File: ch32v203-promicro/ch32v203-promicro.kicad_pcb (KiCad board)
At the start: 2 copper layers, 17.8 x 33 mm, 27 parts, among them J1 USB2.0_C_v3, J2 ProMicro-LeftPin, J3 ProMicro-RightPin, SW1 SW_Push, SW2 SW_Push, U1 CH32V203CxT6, U2 AMS1117-3.3, Y1 32.768k, Y2 8M

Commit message: stm32
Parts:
- added JP1: Jumper_3_Open, Jumper:SolderJumper-3_P1.3mm_Open_RoundedPad1.0x1.5mm, B.Cu at (113.9, 128.3)
- added R8: 10k, $74th:Register_0805_2012, B.Cu at (106.2, 127.6)
- J2: value ProMicro-LeftPin -> ProMicro-LeftPin-NoGND; footprint $74th:ProMicro_LIKE_LEFT -> $74th:ProMicro_LIKE_LEFT_NO_GND
- moved C6 4.83 mm to (109.0, 125.7)
- moved R1 1.81 mm to (106.2, 109.9)
- moved C10 1.27 mm to (113.4, 131.9), turned to 0 degrees
- moved R2 0.86 mm to (112.7, 124.9), turned to 180 degrees
- moved R6 0.46 mm to (103.1, 124.4)
- moved C5 0.35 mm to (108.1, 112.8)
- moved R7 0.35 mm to (106.0, 124.4)
- moved Y2 0.32 mm to (109.0, 130.8)
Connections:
- J2 pad 3: GND -> SWDIO
- J2 pad 4: GND -> SWCLK
- SW1 pad 1: GND -> Net-(JP1-C)
- U1 pad 14: unconnected-(U1-Pad14) -> 10/A10
- U1 pad 34: unconnected-(U1-Pad34) -> SWDIO
- U1 pad 37: unconnected-(U1-Pad37) -> SWCLK
- U1 pad 38: 10/A10 -> unconnected-(U1-PA15-Pad38)
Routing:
- net 10/A10: track 25.2 -> 12.3 mm, vias 1 -> 2
- net GND: track 98.7 -> 86.5 mm, vias 25 -> 23
- net SWDIO: track 0.00 -> 9.83 mm
- net Net-(JP1-C): track 0.00 -> 7.83 mm, vias 0 -> 1
- net SWCLK: track 0.00 -> 7.28 mm
- net RST: track 36.6 -> 40.3 mm, vias 1 -> 3
- net +3V3: track 64.4 -> 67.1 mm
- net Net-(U1-VDDA): track 4.69 -> 2.70 mm
- net 1/UART_TX: track 15.2 -> 16.5 mm
- net DP: track 25.5 -> 24.4 mm
- net 0/UART_RX: track 12.8 -> 13.8 mm
- net Net-(D1-A): track 2.19 -> 2.91 mm
- net 19/A1: track 9.64 -> 10.2 mm
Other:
- board text added: "B"
- board text added: "SELECT BOOT0 R2:3V3 R8:GND"
- board text added: "STM32Micro"
- board text added: "V"
- board text removed: "C32V203Micro"

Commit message: stm32
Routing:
- net GND: track 86.5 -> 89.1 mm
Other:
- board text added: "A4"
- board text added: "A5"
- board text added: "TX1 RX1"
- board text removed: "A15"
- board text removed: "AD0"
- board text removed: "AD1"
- board text removed: "AD2"
- board text removed: "AD3"
- board text removed: "MISO"
- board text removed: "MOSI"
- board text removed: "RX"
- board text removed: "SCK"
- board text removed: "SPI1"
- board text removed: "TX"
- board text removed: "UART1"

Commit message: stm32
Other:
- board text added: "v1.1.0"
- board text removed: "v1.0.0"
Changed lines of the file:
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@@
   (gr_arc (start 101.279026 133.010974) (mid 100.381 132.639) (end 100.009026 131.740974)
     (stroke (width 0.1) (type solid)) (layer "Edge.Cuts"))
-  (gr_text "v1.0.0" (at 111.8 108.7) (layer "B.SilkS")
+  (gr_text "v1.1.0" (at 111.8 108.7) (layer "B.SilkS")
     (effects (font (size 1 1) (thickness 0.15)) (justify mirror))
   )

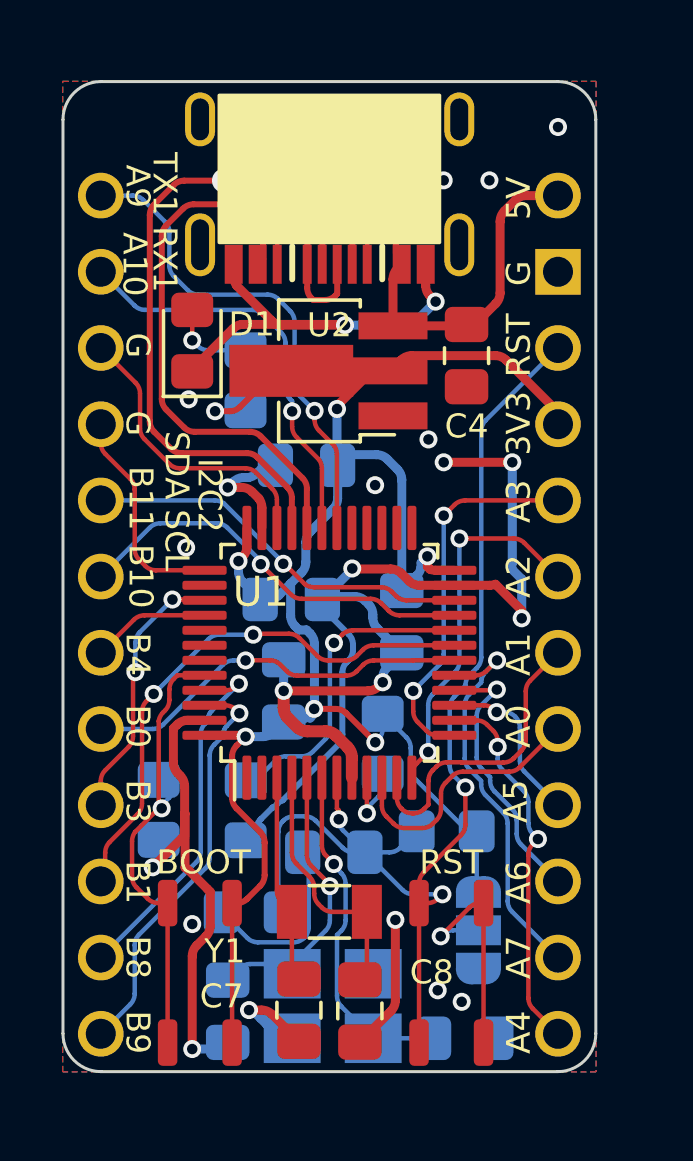
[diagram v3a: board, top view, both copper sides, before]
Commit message: x32micro v1.1.0
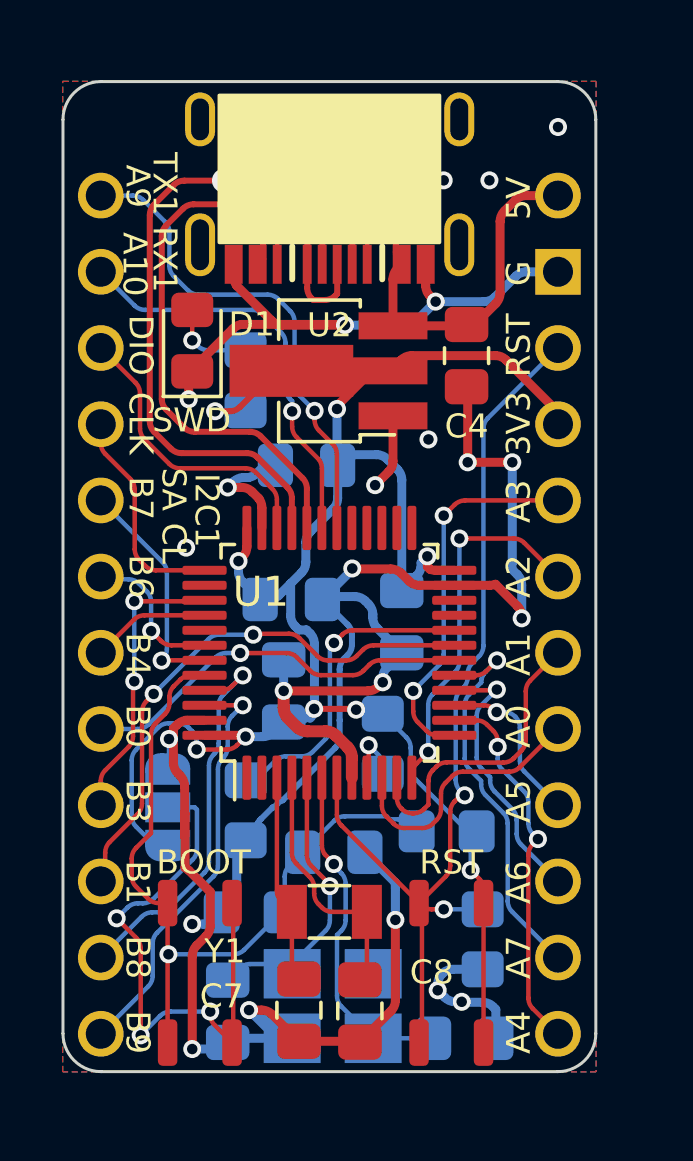
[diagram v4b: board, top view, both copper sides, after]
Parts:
- added REF**: JLCJLCJLCJLC, $74th:JLCJLCJLCJLC, B.Cu at (103.1, 104.4)
- U1: value CH32V203CxT6 -> STM32V103C8T6
- moved R6 11.6 mm to (113.9, 128.7)
- moved JP1 11.1 mm to (103.5, 124.2), turned to -90 degrees
- turned C6 to 0 degrees
- turned SW2 to -90 degrees
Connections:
- net Net-(U1-BOOT1/PB2/UART4_CK) renamed BOOT1
- C6 pad 1: RST -> BOOT0
- R2 pad 2: RST -> BOOT0
- R6 pad 1: Net-(U1-BOOT0) -> RST
- R8 pad 1: RST -> BOOT0
- SW1 pad 1: Net-(JP1-C) -> +3V3
- SW2 pad 1: Net-(U1-BOOT0) -> Net-(JP1-C)
- SW2 pad 2: +3V3 -> BOOT0
- U1 pad 21: 3/I2C_SCL -> unconnected-(U1-PB10/I2C2_SCL/UART3_TX-Pad21)
- U1 pad 22: 2/I2C_SDA -> unconnected-(U1-PB11/I2C2_SDA/UART3_RX-Pad22)
- U1 pad 42: unconnected-(U1-PB6/USB2DM/I2C1_SCL-Pad42) -> 3/I2C_SCL
- U1 pad 43: unconnected-(U1-PB7/USB2DP/I2C1_SDA-Pad43) -> 2/I2C_SDA
- U1 pad 44: Net-(U1-BOOT0) -> BOOT0
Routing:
- net BOOT0: track 0.00 -> 25.0 mm, vias 0 -> 1
- net GND: track 89.1 -> 110.5 mm
- net Net-(U1-BOOT0): track 15.6 -> 0.00 mm, vias 1 -> 0
- net Net-(JP1-C): track 7.83 -> 18.8 mm, vias 1 -> 3
- net 3/I2C_SCL: track 13.7 -> 5.02 mm
- net RST: track 40.3 -> 32.8 mm, vias 3 -> 2
- net 2/I2C_SDA: track 13.1 -> 7.71 mm
- net +3V3: track 67.1 -> 68.5 mm, vias 7 -> 9
- net 8/A8: track 12.2 -> 13.0 mm
- net 6/A7: track 8.85 -> 9.59 mm
- net Net-(U1-PC15/OSC32OUT): track 9.22 -> 8.54 mm
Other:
- board text added: "+"
- board text added: "@74th"
- board text added: "B6"
- board text added: "B7"
- board text added: "BT0Pull R2:3V3 R8:GND"
- board text added: "BTBtn"
- board text added: "CL"
- board text added: "CLK"
- board text added: "DIO"
- board text added: "I2C1"
- board text added: "SA"
- board text added: "SWD"
- board text added: "X32Micro"
- board text added: ""
- board text removed: "B"
- board text removed: "B10"
- board text removed: "B11"
- board text removed: "I2C2"
- board text removed: "SCL"
- board text removed: "SDA"
- board text removed: "SELECT BOOT0 R2:3V3 R8:GND"
- board text removed: "STM32Micro"
- board text removed: "V"

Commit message: v1.2.0
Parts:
- removed C8: 12p, $74th:Capacitor_0805_2012
- removed J2: ProMicro-LeftPin-NoGND, $74th:ProMicro_LIKE_LEFT_NO_GND
- removed J3: ProMicro-RightPin, $74th:ProMicro_LIKE_RIGHT
- removed JP1: Jumper_3_Open, Jumper:SolderJumper-3_P1.3mm_Open_RoundedPad1.0x1.5mm
- removed R3: 0, $74th:Register_0805_2012
- removed R6: 10k, $74th:Register_0805_2012
- removed Y1: 32.768k, $74th:Crystal_SMD_3215-2Pin_3.2x1.5mm
- added C11: 1u, $74th:Capacitor_0805_2012, B.Cu at (110.4, 115.1)
- added J5: ProMicro-LeftPin-NoGND, $74th:ProMicro_LIKE_LEFT_NO_GND, F.Cu at (101.6, 118.1)
- added J6: ProMicro-RightPin, $74th:ProMicro_LIKE_RIGHT, F.Cu at (116.8, 119.4)
- added R9: 27.4, $74th:Register_0805_2012, B.Cu at (108.7, 109.8)
- added U4: CH213K, Package_TO_SOT_SMD:SOT-23, B.Cu at (107.1, 102.5)
- C5: value 2.2u -> 10u
- C7: value 12p -> 100n; moved to B.Cu
- D1: value LED -> BLUE
- R1: value 200 -> 10k
- R2: value 10k -> 27.4
- moved R2 15.2 mm to (110.6, 109.8), turned to -90 degrees
- moved C7 13.6 mm to (107.6, 117.4), turned to 0 degrees
- moved R7 9.70 mm to (113.4, 118.1), turned to 90 degrees
- moved C4 9.55 mm to (103.9, 109.8)
- moved D1 9.28 mm to (113.6, 109.0)
- moved R1 7.44 mm to (113.6, 109.0)
- moved C6 6.06 mm to (113.5, 129.8)
- moved C2 5.75 mm to (111.6, 121.4)
- moved C5 5.42 mm to (113.5, 112.2), turned to 0 degrees
- moved R8 4.32 mm to (103.5, 131.0), turned to -90 degrees
- moved R4 1.99 mm to (109.9, 103.0)
- moved R5 1.90 mm to (111.8, 103.0)
- moved C3 0.82 mm to (107.6, 121.1)
- moved U2 0.54 mm to (109.0, 110.2), turned to 0 degrees
- moved SW1 0.47 mm to (113.3, 130.0)
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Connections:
- net BOOT1 renamed Net-(U1-BOOT1/PB2)
- C4 pad 1: +5V -> Net-(U2-VI)
- C6 pad 1: BOOT0 -> /~{RESET}
- C7 pad 1: Net-(U1-PC14/OSC32IN) -> +3V3
- J1 pad 2: DM -> Net-(J1-D-)
- J1 pad 3: DP -> Net-(J1-D+)
- R2 pad 1: +3V3 -> Net-(J1-D-)
- R2 pad 2: BOOT0 -> /USB_DM
- R8 pad 1: BOOT0 -> Net-(U1-BOOT0)
- SW1 pad 2: RST -> /~{RESET}
- SW2 pad 1: Net-(JP1-C) -> +3V3
- SW2 pad 2: BOOT0 -> Net-(U1-BOOT0)
- U1 pad 1: unconnected-(U1-VBAT-Pad1) -> +3V3
- U1 pad 10: 18/A0 -> /18/A0
- U1 pad 11: 19/A1 -> /19/A1
- U1 pad 12: 20/A2 -> /20/A2
- U1 pad 13: 21/A3 -> /21/A3
- U1 pad 14: 10/A10 -> /10/A10
- U1 pad 15: 15/SPI_SCK -> /15/SPI_SCK
- U1 pad 16: 14/SPI_MISO -> /14/SPI_MISO
- U1 pad 17: 16/SPI_MOSI -> /16/SPI_MOSI
- U1 pad 18: 5 -> /6/A7
- U1 pad 19: 7 -> /4/A6
- U1 pad 3: Net-(U1-PC14/OSC32IN) -> unconnected-(U1-PC14/OSC32IN-Pad3)
- U1 pad 30: 1/UART_TX -> /1/UART_TX
- U1 pad 31: 0/UART_RX -> /0/UART_RX
- U1 pad 32: DM -> /USB_DM
- U1 pad 33: DP -> /USB_DP
- U1 pad 34: SWDIO -> /SWDIO
- U1 pad 37: SWCLK -> /SWCLK
- U1 pad 39: 6/A7 -> /5
- U1 pad 4: Net-(U1-PC15/OSC32OUT) -> unconnected-(U1-PC15/OSC32OUT-Pad4)
- U1 pad 40: 4/A6 -> /7
- U1 pad 42: 3/I2C_SCL -> /3/ISC_SCL
- U1 pad 43: 2/I2C_SDA -> /2/ISC_SDA
- U1 pad 44: BOOT0 -> Net-(U1-BOOT0)
- U1 pad 45: 8/A8 -> /8/A8
- U1 pad 46: 9/A9 -> /9/A9
- U1 pad 7: RST -> /~{RESET}
- U1 pad 9: Net-(U1-VDDA) -> +3V3
- U2 pad 3: +5V -> Net-(U2-VI)
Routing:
- net /~{RESET}: track 0.00 -> 34.2 mm, vias 0 -> 2
- net RST: track 32.8 -> 0.00 mm, vias 2 -> 0
- net DM: track 28.5 -> 0.00 mm, vias 2 -> 0
- net BOOT0: track 25.0 -> 0.00 mm, vias 1 -> 0
- net DP: track 24.4 -> 0.00 mm, vias 2 -> 0
- net Net-(JP1-C): track 18.8 -> 0.00 mm, vias 3 -> 0
- net GND: track 110.5 -> 129.1 mm, vias 23 -> 53
- net Net-(U1-BOOT0): track 0.00 -> 18.3 mm, vias 0 -> 2
- net 7: track 18.2 -> 0.00 mm, vias 2 -> 0
- net /18/A0: track 0.00 -> 17.3 mm, vias 0 -> 3
- net /1/UART_TX: track 0.00 -> 16.5 mm, vias 0 -> 1
- net 1/UART_TX: track 16.5 -> 0.00 mm, vias 1 -> 0
- net /6/A7: track 0.00 -> 15.9 mm, vias 0 -> 1
- net /4/A6: track 0.00 -> 14.5 mm, vias 0 -> 1
- net /0/UART_RX: track 0.00 -> 14.2 mm, vias 0 -> 1
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
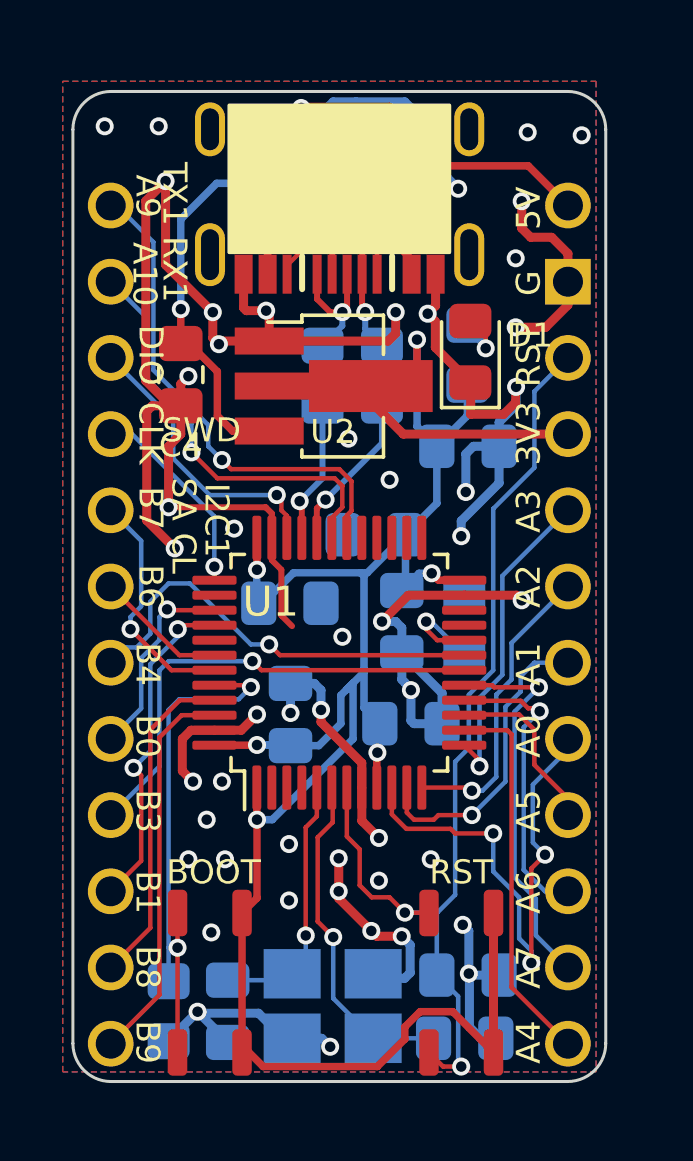
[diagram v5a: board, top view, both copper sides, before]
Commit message: ch32v203 promicro v1.2.1
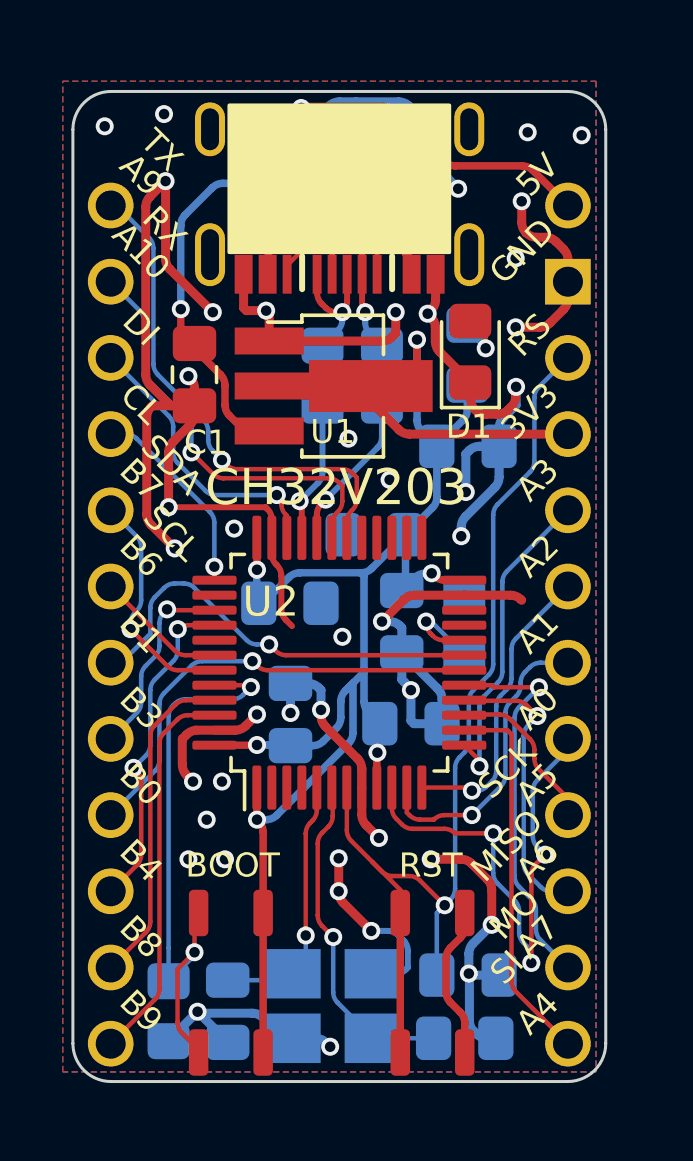
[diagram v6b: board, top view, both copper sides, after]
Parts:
- added MISC-ICON: LOGO, $74th:74th-4mm, B.Cu at (105.7, 110.4)
- U2: renamed from U1; value STM32V103C8T6 -> CH32V203C8T6
- moved REF** 1.24 mm to (103.4, 105.6)
- moved SW2 0.96 mm to (112.3, 130.0), turned to 90 degrees
- moved SW1 0.70 mm to (105.6, 130.0)
- moved C1 0.46 mm to (104.4, 109.8)
- renumbered C4 to C1, C5 to C2, C11 to C3, C7 to C4, C1 to C5, C3 to C6, C2 to C7, C6 to C8, J5 to J2, J6 to J3, R5 to R1, R4 to R2, R1 to R3, R2 to R4, R9 to R5, R7 to R6, R8 to R7, SW2 to SW1, SW1 to SW2, U2 to U1, U4 to U3, Y2 to Y1
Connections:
- SW2 pad 1: +3V3 -> /~{RESET}
- SW2 pad 2: /~{RESET} -> GND
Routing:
- net +3V3: track 74.9 -> 58.5 mm
- net Net-(U1-VI): track 11.6 -> 9.97 mm
- net Net-(U2-BOOT0): track 18.3 -> 19.5 mm
- net /14/SPI_MISO: track 9.92 -> 9.07 mm
- net +5V: track 22.3 -> 21.6 mm
- net /6/A7: track 15.9 -> 15.3 mm
- net Net-(J1-D-): track 5.43 -> 4.80 mm
- net /0/UART_RX: track 14.2 -> 13.5 mm
- net /~{RESET}: track 34.2 -> 34.9 mm, vias 2 -> 1
- net /SWCLK: track 6.72 -> 6.17 mm
- net Net-(D1-A): track 1.98 -> 1.44 mm
- net GND: track 129.1 -> 128.7 mm, vias 53 -> 46
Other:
- board text added: "CH32V203"
- board text added: "DI"
- board text added: "GND"
- board text added: "MISO"
- board text added: "MO"
- board text added: "ProMicro"
- board text added: "RS"
- board text added: "RX"
- board text added: "SCK"
- board text added: "SCL"
- board text added: "SDA"
- board text added: "SI"
- board text added: "TX"
- board text added: "v1.2.1"
- board text removed: "+"
- board text removed: "BT0Pull R2:3V3 R8:GND"
- board text removed: "BTBtn"
- board text removed: "CLK"
- board text removed: "DIO"
- board text removed: "G"
- board text removed: "I2C1"
- board text removed: "SA"
- board text removed: "SWD"
- board text removed: "TX1 RX1"
- board text removed: "X32Micro"
- board text removed: "v1.1.0"
- board text removed: ""

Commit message: update kicad version
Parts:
- C1, C10, C2, C3, C4, C5, C6, C7, C8, C9: footprint $74th:Capacitor_0805_2012 -> 74th:Capacitor_0805_2012
- D1: footprint $74th:LED_0805_2012Metric_Pad1.15x1.40mm_HandSolder -> 74th:LED_0805_2012
- J1: footprint $74th:USB-C-12-Pin-SMD -> 74th:Connector_USB-C-Receptacle_SMT_12-Pin_Simple
- J2: footprint $74th:ProMicro_LIKE_LEFT_NO_GND -> 74th:PinOut_ProMicro-LIKE_LEFT_NO-GND
- J3: footprint $74th:ProMicro_LIKE_RIGHT -> 74th:PinOut_ProMicro-LIKE_RIGHT
- R1, R2, R3, R4, R5, R6, R7: footprint $74th:Register_0805_2012 -> 74th:Register_0805_2012
- SW1, SW2: footprint $74th:SKRPABE010 -> 74th:Switch_SKRPABE010
- U1: footprint Package_TO_SOT_SMD:SOT-89-3_Handsoldering -> 74th:Package_SOT-89-3
- U2: footprint Package_QFP:LQFP-48_7x7mm_P0.5mm -> 74th:Package_LQFP-48_7x7mm_P0.5mm
- U3: footprint Package_TO_SOT_SMD:SOT-23 -> 74th:Package_SOT-23
- Y1: footprint $74th:Crystal_SMD_3225-4Pin_3.2x2.5mm_HandSoldering -> 74th:Crystal_SMD_3225-4Pin_3.2x2.5mm_HandSoldering
- moved U1 0.54 mm to (109.0, 110.7)
- moved R2 0.08 mm to (109.8, 103.0)
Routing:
- net GND: track 128.7 -> 165.2 mm, vias 46 -> 68
- net Net-(J1-D-): track 4.80 -> 8.46 mm
- net Net-(J1-D+): track 4.48 -> 7.09 mm, vias 1 -> 2
- net +5V: track 21.6 -> 24.0 mm
- net Net-(J1-CC2): track 3.13 -> 4.84 mm
- net Net-(U2-BOOT0): track 19.5 -> 18.2 mm
- net /~{RESET}: track 34.9 -> 33.8 mm
- net Net-(J1-CC1): track 2.89 -> 3.94 mm
- net Net-(U1-VI): track 9.97 -> 10.7 mm
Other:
- board text added: "v${REVISION}"
- board text removed: "BOOT"
- board text removed: "RST"
- board text removed: "v1.2.1"

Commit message: fix
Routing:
- net Net-(U2-BOOT0): track 18.2 -> 19.9 mm
